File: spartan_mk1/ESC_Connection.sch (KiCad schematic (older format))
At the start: 4 parts, among them J15 Conn_01x08_Female, J16 Conn_01x02_Female, J17 Conn_01x02_Female, J18 Conn_01x08_Female

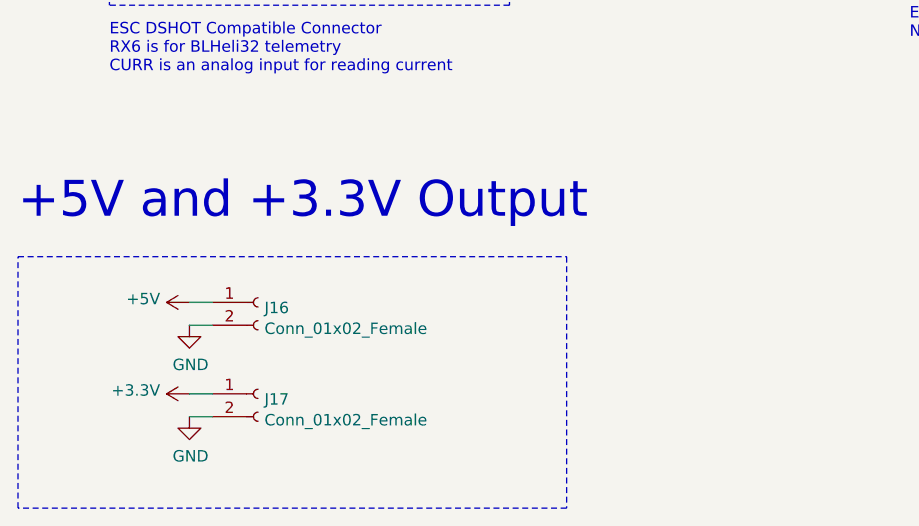
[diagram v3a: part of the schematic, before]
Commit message: Almost complete PCB layout (no routing)
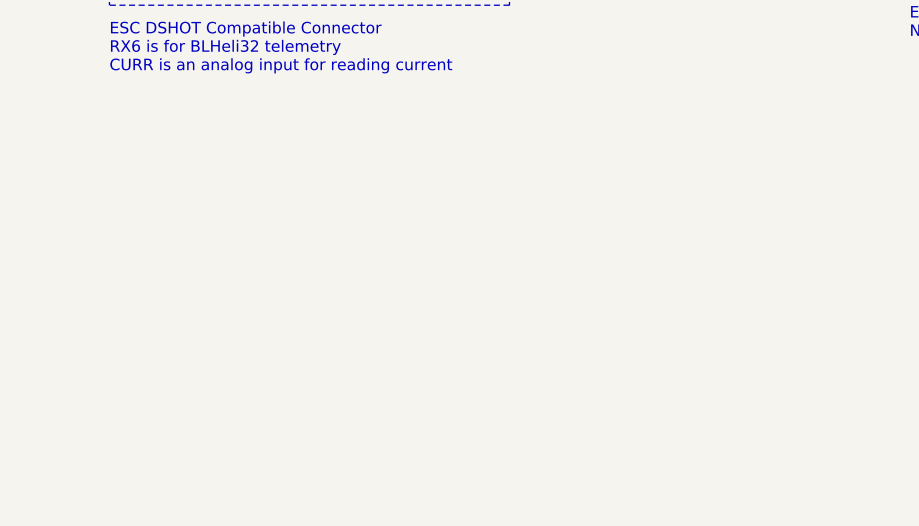
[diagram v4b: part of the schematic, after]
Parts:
- removed J16, J17: Conn_01x02_Female, Connector_PinHeader_2.54mm:PinHeader_1x02_P2.54mm_Vertical, symbol Connector:Conn_01x02_Female
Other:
- note removed: "+5V and +3.3V Output"
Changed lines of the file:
@@
 	-1   0    0    -1
-$EndComp
-$Comp
-L Connector:Conn_01x02_Female J?
-U 1 1 5F94A9E6
-P 4000 5200
-AR Path="/5F78701C/5F94A9E6" Ref="J?"  Part="1"
-AR Path="/5F79A745/5F94A9E6" Ref="J?"  Part="1"
-AR Path="/5FB6E842/5F94A9E6" Ref="J16"  Part="1"
-F 0 "J16" H 4028 5176 50  0000 L CNN
-F 1 "Conn_01x02_Female" H 4028 5085 50  0000 L CNN
-F 2 "Connector_PinHeader_2.54mm:PinHeader_1x02_P2.54mm_Vertical" H 4000 5200 50  0001 C CNN
-F 3 "~" H 4000 5200 50  0001 C CNN
-	1    4000 5200
-	1    0    0    -1
-$EndComp
-$Comp
-L Connector:Conn_01x02_Female J?
-U 1 1 5F94A9EC
-P 4000 5600
-AR Path="/5F78701C/5F94A9EC" Ref="J?"  Part="1"
-AR Path="/5F79A745/5F94A9EC" Ref="J?"  Part="1"
-AR Path="/5FB6E842/5F94A9EC" Ref="J17"  Part="1"
-F 0 "J17" H 4028 5576 50  0000 L CNN
-F 1 "Conn_01x02_Female" H 4028 5485 50  0000 L CNN
-F 2 "Connector_PinHeader_2.54mm:PinHeader_1x02_P2.54mm_Vertical" H 4000 5600 50  0001 C CNN
-F 3 "~" H 4000 5600 50  0001 C CNN
-	1    4000 5600
-	1    0    0    -1
-$EndComp
-Wire Wire Line
-	3700 5200 3800 5200
-Wire Wire Line
-	3800 5600 3700 5600
-$Comp
-L power:GND #PWR?
-U 1 1 5F94A9F4
-P 3700 5300
-AR Path="/5F78701C/5F94A9F4" Ref="#PWR?"  Part="1"
-AR Path="/5F79A745/5F94A9F4" Ref="#PWR?"  Part="1"
-AR Path="/5FB6E842/5F94A9F4" Ref="#PWR067"  Part="1"
-F 0 "#PWR067" H 3700 5050 50  0001 C CNN
-F 1 "GND" H 3705 5127 50  0000 C CNN
-F 2 "" H 3700 5300 50  0001 C CNN
-F 3 "" H 3700 5300 50  0001 C CNN
-	1    3700 5300
-	1    0    0    -1
-$EndComp
-$Comp
-L power:GND #PWR?
-U 1 1 5F94A9FA
-P 3700 5700
-AR Path="/5F78701C/5F94A9FA" Ref="#PWR?"  Part="1"
-AR Path="/5F79A745/5F94A9FA" Ref="#PWR?"  Part="1"
-AR Path="/5FB6E842/5F94A9FA" Ref="#PWR069"  Part="1"
-F 0 "#PWR069" H 3700 5450 50  0001 C CNN
-F 1 "GND" H 3705 5527 50  0000 C CNN
-F 2 "" H 3700 5700 50  0001 C CNN
-F 3 "" H 3700 5700 50  0001 C CNN
-	1    3700 5700
-	1    0    0    -1
-$EndComp
-Wire Wire Line
-	3800 5700 3700 5700
-Wire Wire Line
-	3700 5300 3800 5300
-$Comp
-L power:+5V #PWR?
-U 1 1 5F94AA02
-P 3700 5200
-AR Path="/5F78701C/5F94AA02" Ref="#PWR?"  Part="1"
-AR Path="/5F79A745/5F94AA02" Ref="#PWR?"  Part="1"
-AR Path="/5FB6E842/5F94AA02" Ref="#PWR066"  Part="1"
-F 0 "#PWR066" H 3700 5050 50  0001 C CNN
-F 1 "+5V" V 3715 5328 50  0000 L CNN
-F 2 "" H 3700 5200 50  0001 C CNN
-F 3 "" H 3700 5200 50  0001 C CNN
-	1    3700 5200
-	0    -1   -1   0
-$EndComp
-$Comp
-L power:+3.3V #PWR?
-U 1 1 5F94AA08
-P 3700 5600
-AR Path="/5F78701C/5F94AA08" Ref="#PWR?"  Part="1"
-AR Path="/5F79A745/5F94AA08" Ref="#PWR?"  Part="1"
-AR Path="/5FB6E842/5F94AA08" Ref="#PWR068"  Part="1"
-F 0 "#PWR068" H 3700 5450 50  0001 C CNN
-F 1 "+3.3V" V 3715 5728 50  0000 L CNN
-F 2 "" H 3700 5600 50  0001 C CNN
-F 3 "" H 3700 5600 50  0001 C CNN
-	1    3700 5600
-	0    -1   -1   0
 $EndComp
 Wire Notes Line
@@
 Wire Notes Line
 	6650 2450 8450 2450
-Text Notes 2950 4850 0    157  ~ 0
-+5V and +3.3V Output
-Wire Notes Line
-	2950 5000 5350 5000
-Wire Notes Line
-	5350 5000 5350 6100
-Wire Notes Line
-	5350 6100 2950 6100
-Wire Notes Line
-	2950 6100 2950 5000
 $Comp
 L power:GND #PWR?
